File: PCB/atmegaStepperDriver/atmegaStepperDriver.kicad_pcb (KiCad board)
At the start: 2 copper layers, 80 parts, among them J1 General power, J2 Motor Output, J3 Motor power, J4 FanSocket, J5 Reset Header, J6 I2C Communication pins, J8 Programming socket 01x06, J9 Stepper communication pins, Q1 TIP42C, Q10 BC557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

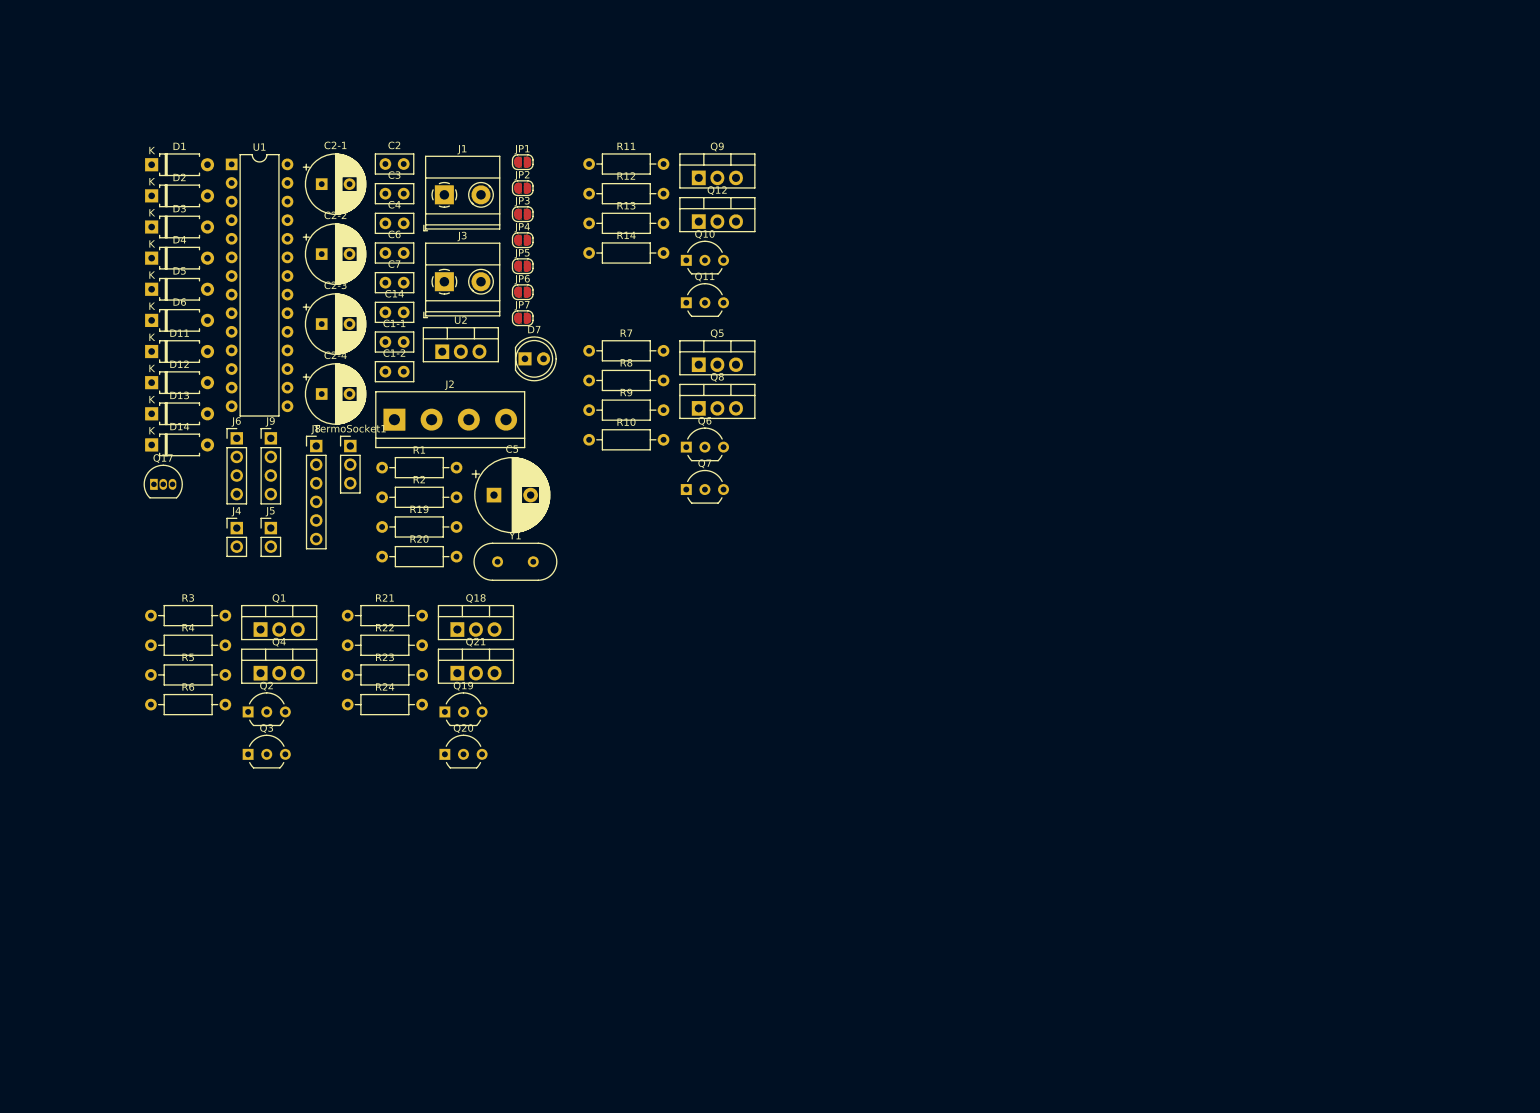
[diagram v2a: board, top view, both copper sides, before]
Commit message: Added analog read for motor error
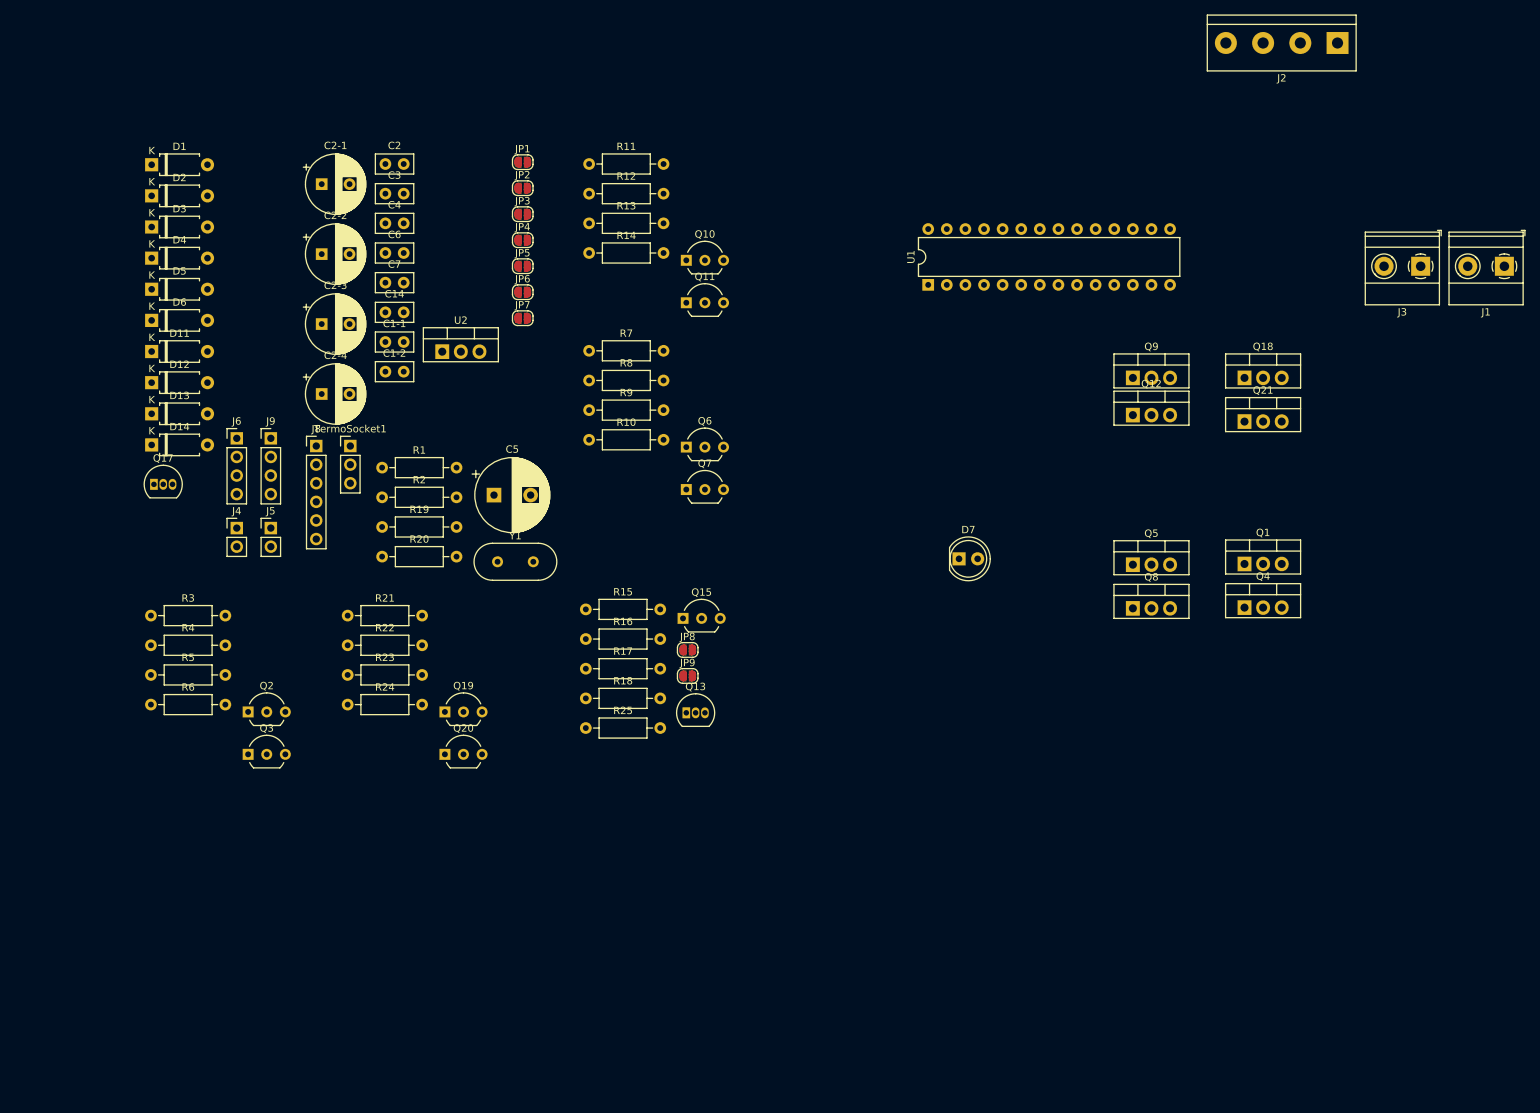
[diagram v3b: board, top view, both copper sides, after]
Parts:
- added JP8: SolderJumper_2_Open, Jumper:SolderJumper-2_P1.3mm_Open_RoundedPad1.0x1.5mm, F.Cu at (145.0, 108.3)
- added JP9: SolderJumper_2_Open, Jumper:SolderJumper-2_P1.3mm_Open_RoundedPad1.0x1.5mm, F.Cu at (145.0, 111.8)
- added Q13: BC547, Package_TO_SOT_THT:TO-92_Inline, F.Cu at (144.8, 116.8)
- added Q15: BC557, Package_TO_SOT_THT:TO-92_Inline_Wide, F.Cu at (144.3, 104.0)
- added R15: 250, Resistor_THT:R_Axial_DIN0207_L6.3mm_D2.5mm_P10.16mm_Horizontal, F.Cu at (131.1, 102.7)
- added R16: 82k, Resistor_THT:R_Axial_DIN0207_L6.3mm_D2.5mm_P10.16mm_Horizontal, F.Cu at (131.1, 106.8)
- added R17: 4.3k, Resistor_THT:R_Axial_DIN0207_L6.3mm_D2.5mm_P10.16mm_Horizontal, F.Cu at (131.1, 110.8)
- added R18: 220, Resistor_THT:R_Axial_DIN0207_L6.3mm_D2.5mm_P10.16mm_Horizontal, F.Cu at (131.1, 114.9)
- added R25: 220, Resistor_THT:R_Axial_DIN0207_L6.3mm_D2.5mm_P10.16mm_Horizontal, F.Cu at (131.1, 118.9)
- moved J1 145.0 mm to (256.5, 55.9), turned to 180 degrees
- moved J2 138.6 mm to (233.7, 25.4), turned to 180 degrees
- moved Q1 134.6 mm to (221.0, 96.5)
- moved Q4 134.6 mm to (221.0, 102.5)
- moved J3 133.3 mm to (245.0, 55.9), turned to 180 degrees
- moved Q18 112.8 mm to (221.0, 71.1)
- moved Q21 112.8 mm to (221.0, 77.1)
- moved U1 96.5 mm to (177.8, 58.4), turned to 90 degrees
- moved Q5 65.2 mm to (205.7, 96.6)
- moved Q8 65.2 mm to (205.7, 102.6)
- moved Q9 65.2 mm to (205.7, 71.1)
- moved D7 65.2 mm to (182.0, 95.8)
- moved Q12 64.9 mm to (205.7, 76.2)
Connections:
- net VCCInput renamed Net-(D5-K)
- net output !A renamed Isolated Read
- U1 pad 23: unconnected-(U1-PC0-Pad23) -> Net-(JP8-B)
- U1 pad 24: unconnected-(U1-PC1-Pad24) -> Net-(JP9-B)

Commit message: someData; idk what i did, forgot to push it
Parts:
- removed D6: D, Diode_THT:D_A-405_P7.62mm_Horizontal
- removed J4: FanSocket, Connector_PinHeader_2.54mm:PinHeader_1x02_P2.54mm_Vertical
- removed JP7: SolderJumper_2_Open, Jumper:SolderJumper-2_P1.3mm_Open_RoundedPad1.0x1.5mm
- removed R15: 250, Resistor_THT:R_Axial_DIN0207_L6.3mm_D2.5mm_P10.16mm_Horizontal
- added 5V_R1: 250, Resistor_THT:R_Axial_DIN0207_L6.3mm_D2.5mm_P10.16mm_Horizontal, F.Cu at (115.1, 140.9)
- added AP_JP1: SolderJumper_2_Open, Jumper:SolderJumper-2_P1.3mm_Open_RoundedPad1.0x1.5mm, F.Cu at (145.8, 123.6)
- added C1: C, Capacitor_THT:CP_Radial_D8.0mm_P3.80mm, F.Cu at (102.4, 135.4)
- added D10: D, Diode_THT:D_DO-35_SOD27_P10.16mm_Horizontal, F.Cu at (122.7, 100.3)
- added D15: D, Diode_THT:D_DO-35_SOD27_P10.16mm_Horizontal, F.Cu at (145.3, 101.3)
- added D16: D, Diode_THT:D_DO-35_SOD27_P10.16mm_Horizontal, F.Cu at (73.7, 100.6)
- added D17: D, Diode_THT:D_DO-35_SOD27_P10.16mm_Horizontal, F.Cu at (97.3, 100.3)
- added D18: D, Diode_THT:D_DO-35_SOD27_P10.16mm_Horizontal, F.Cu at (120.1, 100.5)
- added D19: D, Diode_THT:D_DO-35_SOD27_P10.16mm_Horizontal, F.Cu at (142.9, 101.6)
- added D8: D, Diode_THT:D_DO-35_SOD27_P10.16mm_Horizontal, F.Cu at (76.2, 100.6)
- added D9: D, Diode_THT:D_DO-35_SOD27_P10.16mm_Horizontal, F.Cu at (99.8, 100.1)
- added FanSocket1: FanSocket, Connector_PinHeader_2.54mm:PinHeader_1x02_P2.54mm_Vertical, F.Cu at (115.6, 163.1)
- added G***: LOGO, Logo:15x15Logo, F.Cu at (127.8, 160.8)
- added GND_R1: 250, Resistor_THT:R_Axial_DIN0207_L6.3mm_D2.5mm_P10.16mm_Horizontal, F.Cu at (111.8, 151.1)
- added MP_JP1: SolderJumper_2_Open, Jumper:SolderJumper-2_P1.3mm_Open_RoundedPad1.0x1.5mm, F.Cu at (148.3, 123.6)
- added M_JP1: SolderJumper_2_Open, Jumper:SolderJumper-2_P1.3mm_Open_RoundedPad1.0x1.5mm, F.Cu at (71.9, 158.1)
- added m_D1: D, Diode_THT:D_A-405_P7.62mm_Horizontal, F.Cu at (75.3, 154.9)
- Q15: footprint Package_TO_SOT_THT:TO-92_Inline_Wide -> Package_TO_SOT_THT:TO-92_Inline
- moved J1 198.5 mm to (87.1, 159.5), turned to 0 degrees
- moved J3 179.6 mm to (98.4, 159.5), turned to 0 degrees
- moved Q18 159.7 mm to (65.0, 105.7)
- moved Q21 159.5 mm to (65.0, 110.7)
- moved J2 158.1 mm to (142.2, 154.4), turned to 90 degrees
- moved U1 142.6 mm to (61.2, 140.5)
- moved Q1 132.4 mm to (88.9, 105.2)
- moved Q4 132.3 mm to (88.9, 110.2)
- moved D11 114.0 mm to (135.1, 162.3)
- moved C6 113.6 mm to (145.8, 159.6), turned to -90 degrees
- moved D4 108.0 mm to (78.8, 162.6), turned to 90 degrees
- moved C14 107.8 mm to (60.2, 160.8), turned to 180 degrees
- moved D12 107.7 mm to (135.1, 158.9)
- moved C2 105.7 mm to (91.0, 146.8)
- moved D2 105.5 mm to (97.5, 148.6), turned to 90 degrees
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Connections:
- Q10 pad 3: +5V -> /GateSheet/Power 5v
- Q19 pad 3: +5V -> /GateSheet/Power 5v
- Q2 pad 3: +5V -> /GateSheet/Power 5v
- Q6 pad 3: +5V -> /GateSheet/Power 5v
- R25 pad 1: Gate 1 -> activeRead
- U1 pad 18: unconnected-(U1-PB4-Pad18) -> activeRead
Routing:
- net Motor Power: track 0.00 -> 218.0 mm, vias 0 -> 5
- net +5V: track 0.00 -> 168.1 mm, vias 0 -> 1
- net output A: track 0.00 -> 158.5 mm
- net Isolated Read: track 0.00 -> 146.4 mm, vias 0 -> 2
- net output !B: track 0.00 -> 118.5 mm, vias 0 -> 2
- net output B: track 0.00 -> 113.7 mm, vias 0 -> 1
- net /GateSheet/Power 5v: track 0.00 -> 82.2 mm, vias 0 -> 1
- net Jumper To lower Pins: track 0.00 -> 78.3 mm, vias 0 -> 2
- net Reader: track 0.00 -> 66.1 mm, vias 0 -> 4
- net activeRead: track 0.00 -> 50.3 mm, vias 0 -> 3
- net GND: track 0.00 -> 44.8 mm, vias 0 -> 12
- net Rotation: track 0.00 -> 40.0 mm
- net Net-(JP3-B): track 0.00 -> 35.7 mm
- net Net-(D5-K): track 0.00 -> 32.2 mm
- net RXD: track 0.00 -> 30.4 mm
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- added copper zone on B.Cu, net GND
- added copper zone on F.Cu, net GND
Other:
- board outline added: 94.5 x 67.6 mm
- board text added: "AtmegaStepperDriver Alpha V0.8.4 by eGuardianDev"
